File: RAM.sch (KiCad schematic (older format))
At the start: 2 parts, among them U1 STM32MP151AAB3, U2 MT41K64M16TW-107_AAT_J_TR

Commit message: Finish labelling RAM
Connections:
- net UDQS_N: now reaches U2.B7 (*UDQS)
- net UDQS: now reaches U2.C7 (UDQS)
- net UDM: now reaches U2.D3 (UDM)
- net LDM: now reaches U2.E7 (LDM)
- net LDQS_P: now reaches U2.F3 (LDQS)
- net LDQS_N: now reaches U2.G3 (*LDQS)
- net VREFDQ: now reaches U2.H1 (VREFDQ)
- net RAS_N: now reaches U2.J3 (*RAS)
- net CK_P: now reaches U2.J7 (CK)
- net ODT: now reaches U2.K1 (ODT)
- net ODT: now also U1.H19 (DDR_ODT)
- net CAS_N: now reaches U2.K3 (*CAS)
- net CK_N: now reaches U2.K7 (*CK)
- net CKE: now reaches U2.K9 (CKE)
- net CKE: now also U1.P19 (DDR_CKE)
- net CS_N: now reaches U2.L2 (*CS)
- net CS_N: now also U1.J18 (DDR_CSN)
- net WE_N: now reaches U2.L3 (*WE)
- net WE_N: now also U1.J17 (DDR_WEN)
- net ZQ: now reaches U2.L8 (ZQ)
- net ZQ: now also U1.F18 (DDR_ZQ)
- net VREFCA: now reaches U2.M8 (VREFCA)
- net RESET_N: now reaches U2.T2 (*RESET)
- net RESET_N: now also U1.G16 (DDR_RESETN)
- net VDD renamed VDDR
- no-connect marks 0 -> 1
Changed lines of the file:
@@
 U 1 1 60175F93
 P 1000 1400
-F 0 "U?" H 2600 1887 60  0000 C CNN
+F 0 "U2" H 2600 1887 60  0000 C CNN
 F 1 "MT41K64M16TW-107_AAT_J_TR" H 2600 1781 60  0000 C CNN
 F 2 "LinuxBoard:MT41K64M16TW-107_AAT_J_TR" H 2600 1740 60  0001 C CNN
@@
 AR Path="/601728E9/6049E2E1" Ref="U?"  Part="4"
 AR Path="/60172A77/6049E2E1" Ref="U1"  Part="4"
-F 0 "U?" H 9400 1787 60  0000 C CNN
+F 0 "U1" H 9400 1787 60  0000 C CNN
 F 1 "STM32MP151AAB3" H 9400 1681 60  0000 C CNN
 F 2 "LinuxBoard:STM32MP151AAB3" H 8550 1640 60  0001 C CNN
@@
 AR Path="/601728E9/6049E2E7" Ref="U?"  Part="3"
 AR Path="/60172A77/6049E2E7" Ref="U1"  Part="3"
-F 0 "U?" H 6150 1787 60  0000 C CNN
+F 0 "U1" H 6150 1787 60  0000 C CNN
 F 1 "STM32MP151AAB3" H 6150 1681 60  0000 C CNN
 F 2 "LinuxBoard:STM32MP151AAB3" H 5950 1640 60  0001 C CNN
@@
 	1350 7100 1350 7200
 $Comp
-L power:GND #PWR011
+L power:GND #PWR0101
 U 1 1 60844341
 P 1350 7200
-F 0 "#PWR?" H 1350 6950 50  0001 C CNN
+F 0 "#PWR0101" H 1350 6950 50  0001 C CNN
 F 1 "GND" H 1355 7027 50  0000 C CNN
 F 2 "" H 1350 7200 50  0001 C CNN
@@
 Text Label 1000 3200 2    50   ~ 0
 VDDQ
-Text Label 2100 7100 2    50   ~ 0
+Text Label 2200 7100 2    50   ~ 0
 VDD
 Text Label 1000 5400 2    50   ~ 0
@@
 	1000 7100 1000 7200
 $Comp
-L power:GND #PWR010
+L power:GND #PWR0102
 U 1 1 60E94F4D
 P 1000 7200
-F 0 "#PWR?" H 1000 6950 50  0001 C CNN
+F 0 "#PWR0102" H 1000 6950 50  0001 C CNN
 F 1 "GND" H 1005 7027 50  0000 C CNN
 F 2 "" H 1000 7200 50  0001 C CNN
@@
 	1    0    0    -1
 $EndComp
+Text Label 4200 5800 0    50   ~ 0
+CK_P
+Text Label 4200 5200 0    50   ~ 0
+CK_N
+Text Label 4200 5300 0    50   ~ 0
+CAS_N
+Text Label 4200 4700 0    50   ~ 0
+WE_N
+Text Label 4200 4800 0    50   ~ 0
+CS_N
+Text Label 1000 2400 2    50   ~ 0
+UDQS_N
+Text Label 1000 3500 2    50   ~ 0
+UDM
+Text Label 1000 3000 2    50   ~ 0
+UDQS
+Text Label 1000 4200 2    50   ~ 0
+LDM
+Text Label 1000 4700 2    50   ~ 0
+LDQS_P
+Text Label 1000 5300 2    50   ~ 0
+LDQS_N
+Text Label 4200 5900 0    50   ~ 0
+RAS_N
+Text Label 4200 5500 0    50   ~ 0
+ODT
+Text Label 4200 5000 0    50   ~ 0
+CKE
+Text HLabel 2400 7100 2    50   Input ~ 0
+VDDR
+Wire Wire Line
+	2400 7100 2200 7100
+Text Label 1000 5700 2    50   ~ 0
+VREFDQ
+NoConn ~ 1000 1400
+Text Label 4200 1800 0    50   ~ 0
+RESET_N
+Text Label 4200 3900 0    50   ~ 0
+VREFCA
+Text Label 4200 4500 0    50   ~ 0
+ZQ
+Text Label 8050 3500 2    50   ~ 0
+RESET_N
+Text Label 8050 1400 2    50   ~ 0
+ZQ
+Text Label 8050 1800 2    50   ~ 0
+CKE
+Text Label 8050 2400 2    50   ~ 0
+WE_N
+Text Label 8050 2200 2    50   ~ 0
+ODT
+Text Label 8050 2000 2    50   ~ 0
+CS_N
 $EndSCHEMATC

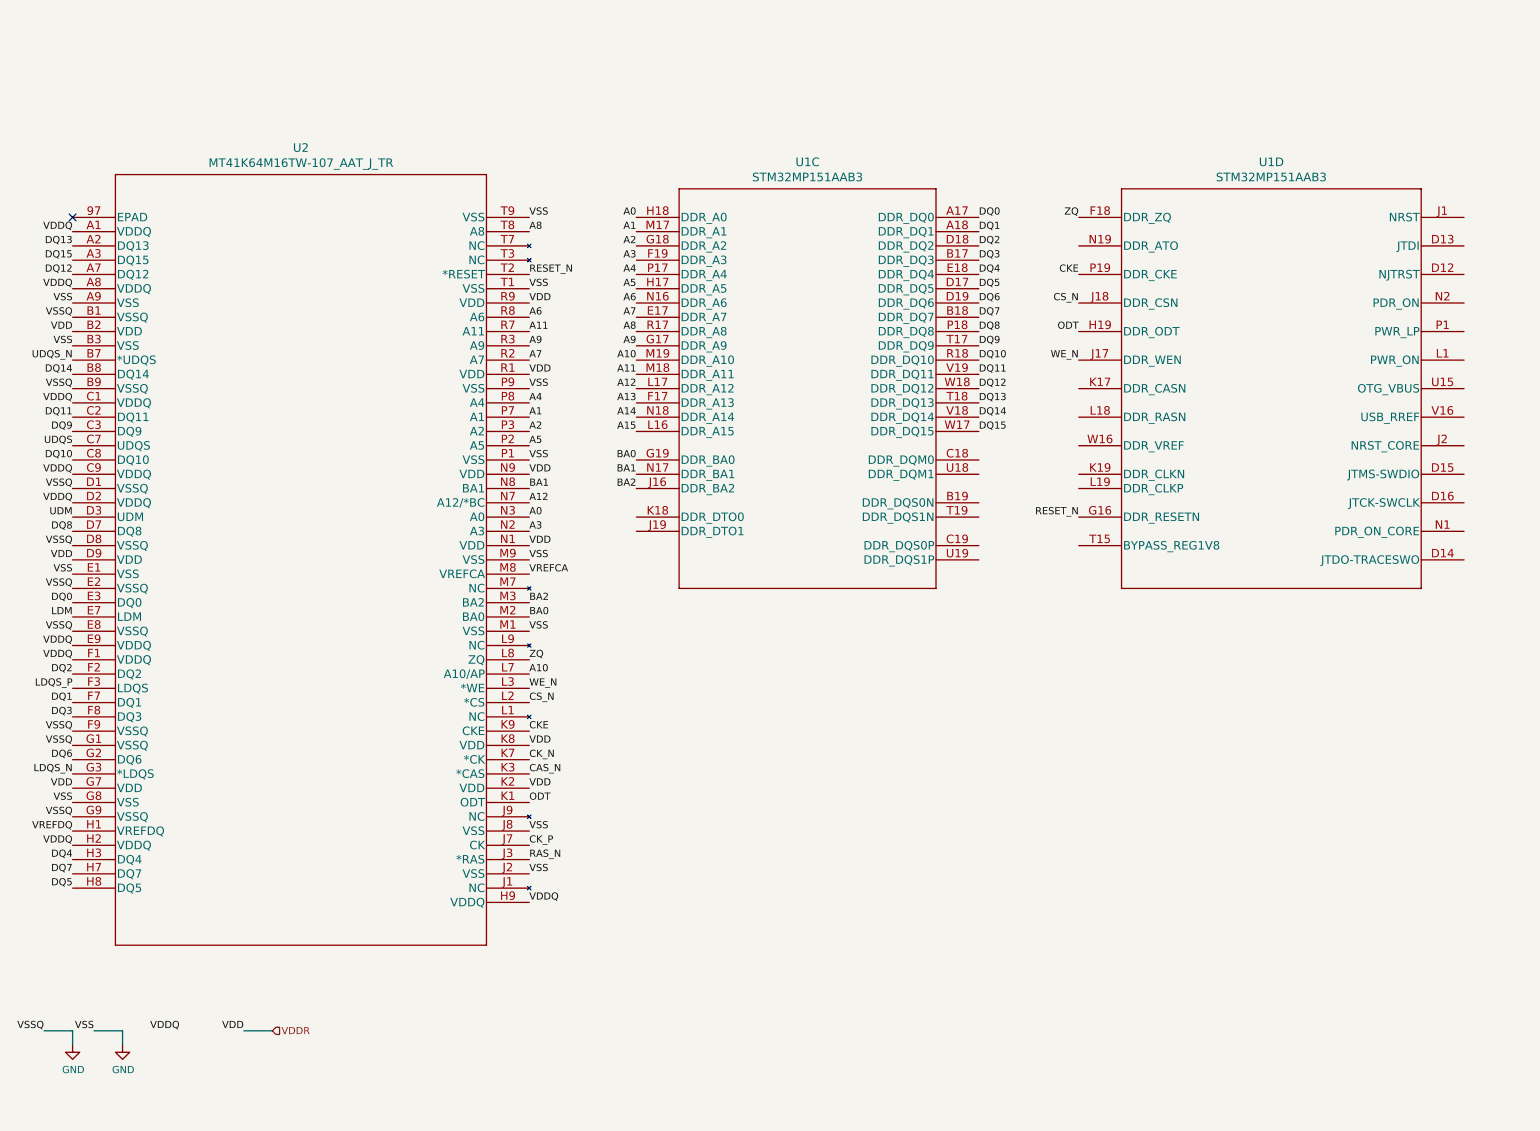
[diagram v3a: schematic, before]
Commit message: Finish DDR schematic
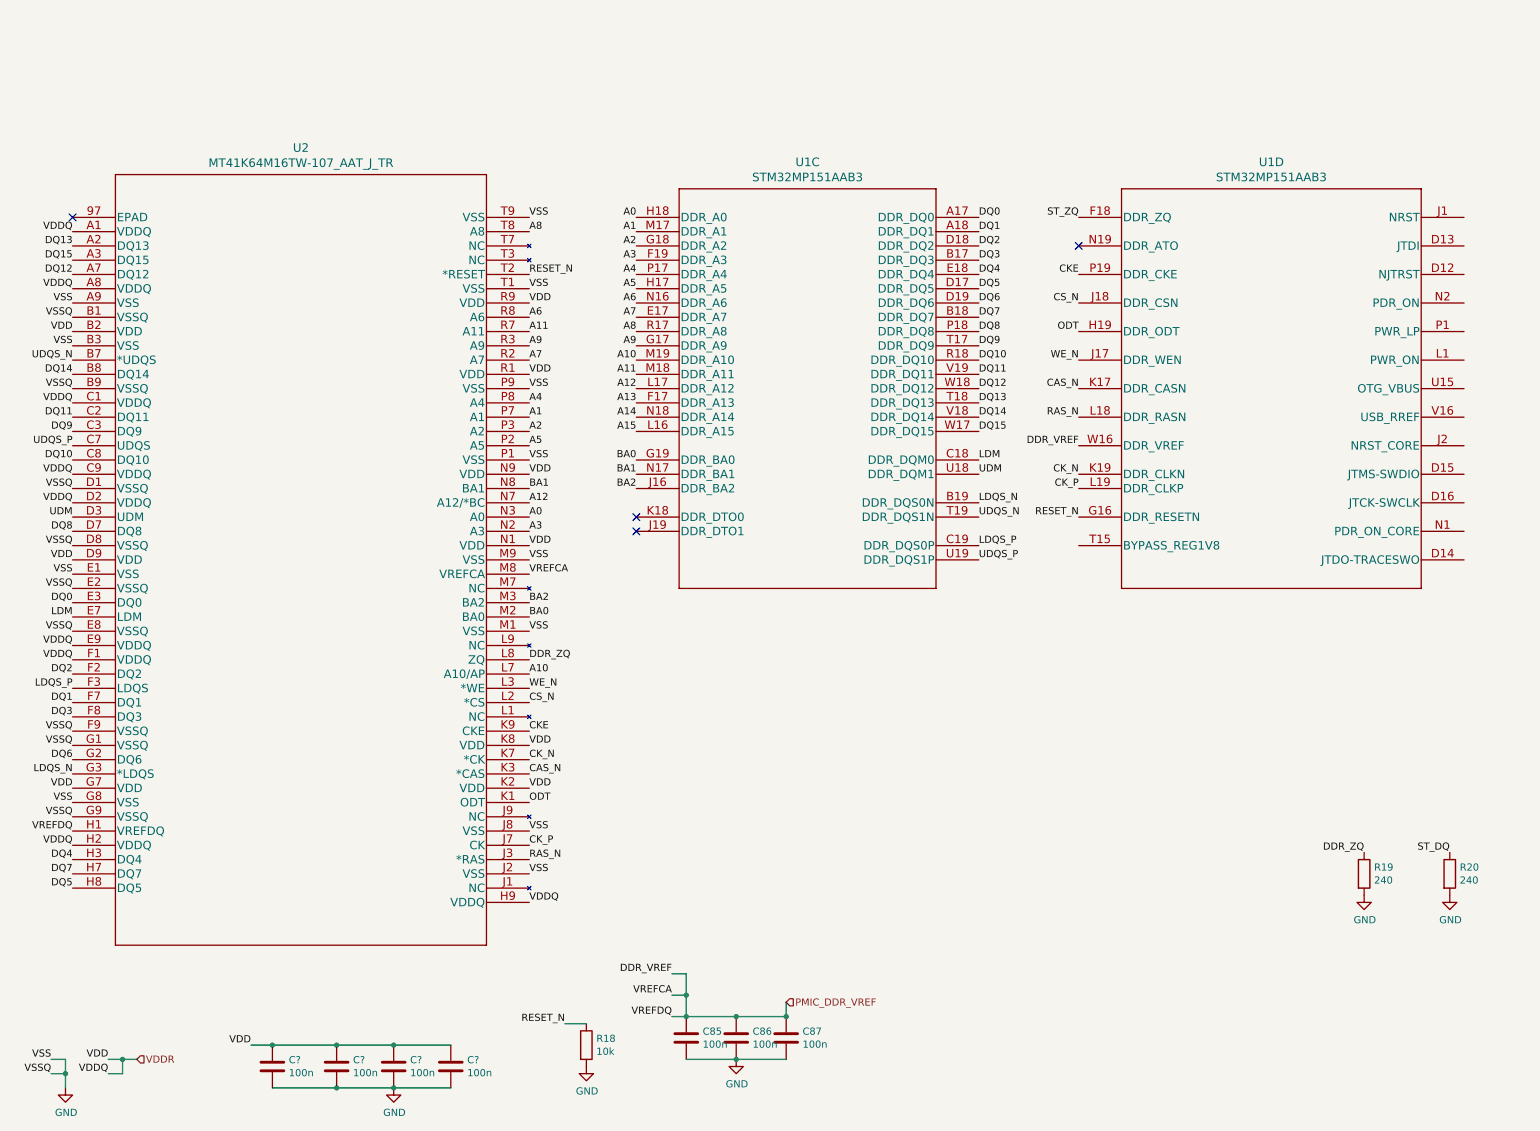
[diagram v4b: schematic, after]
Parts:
- added C85, C86, C87, C? (x4): 100n, symbol Device:C
- added R18: 10k, symbol Device:R
- added R19, R20: 240, symbol Device:R
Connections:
- net UDQS is gone; now on net UDQS_P: U2.C7 (UDQS)
- net VDDQ is gone; now on net VDDR: U2.A1 (VDDQ), U2.A8 (VDDQ), U2.C1 (VDDQ), U2.C9 (VDDQ), U2.D2 (VDDQ), U2.E9 (VDDQ), U2.F1 (VDDQ), U2.H2 (VDDQ), U2.H9 (VDDQ)
- net VREFCA is gone; now on net PMIC_DDR_VREF: U2.M8 (VREFCA)
- net VREFDQ is gone; now on net PMIC_DDR_VREF: U2.H1 (VREFDQ)
- net CAS_N: now also U1.K17 (DDR_CASN)
- net CK_N: now also U1.K19 (DDR_CLKN)
- net CK_P: now also U1.L19 (DDR_CLKP)
- net GND: now also C85.2, C86.2, C87.2, C?.2, C?.2, C?.2, C?.2, R18.2, R19.2, R20.2
- net LDM: now also U1.C18 (DDR_DQM0)
- net LDQS_N: now also U1.B19 (DDR_DQS0N)
- net LDQS_P: now also U1.C19 (DDR_DQS0P)
- net RAS_N: now also U1.L18 (DDR_RASN)
- net RESET_N: now also R18.1
- net UDM: now also U1.U18 (DDR_DQM1)
- net UDQS_N: now also U1.T19 (DDR_DQS1N)
- net VDDR: now also C?.1, C?.1, C?.1, C?.1
- net PMIC_DDR_VREF: now reaches U1.W16 (DDR_VREF)
- net PMIC_DDR_VREF: now also C85.1, C86.1, C87.1
- net UDQS_P: now reaches U1.U19 (DDR_DQS1P)
- net ZQ renamed DDR_ZQ
- net DDR_ZQ: now also R19.1; no longer U1.F18 (DDR_ZQ)
- new net ST_DQ: R20.1
- new net ST_ZQ: U1.F18 (DDR_ZQ)
- no-connect marks 1 -> 4

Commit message: Complete gpio selection, tidy sheets
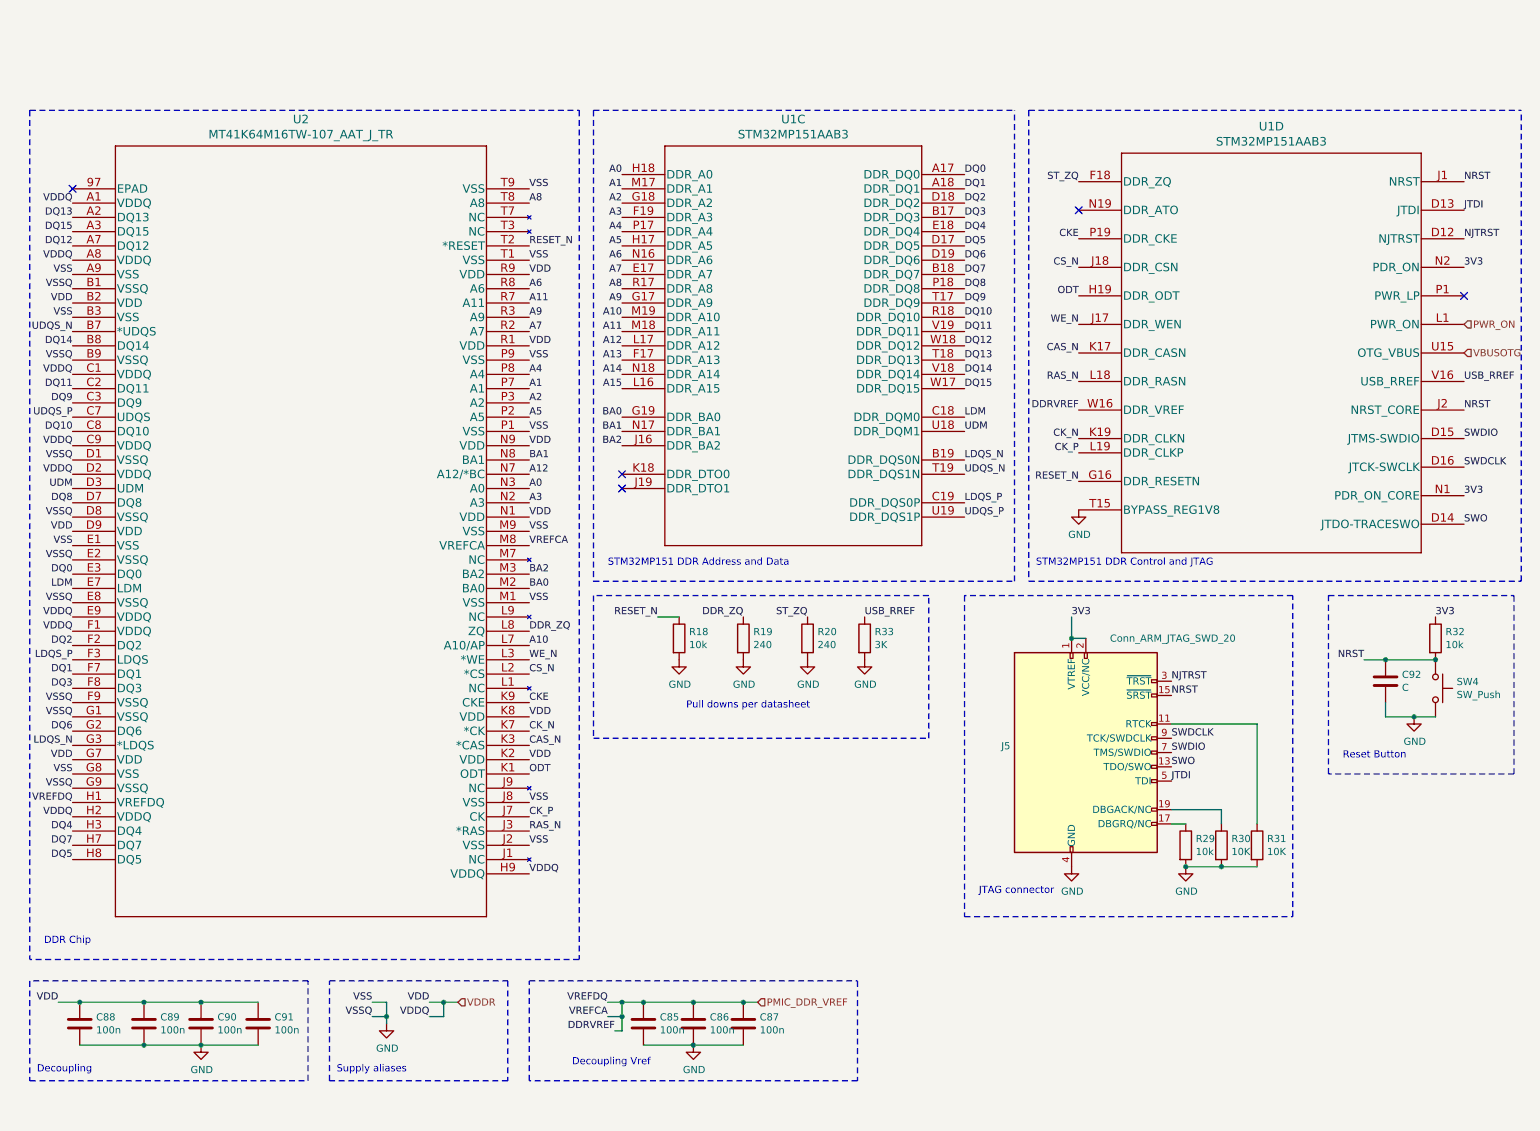
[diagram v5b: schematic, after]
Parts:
- added C92: C, symbol Device:C
- added J5: Conn_ARM_JTAG_SWD_20, symbol Connector:Conn_ARM_JTAG_SWD_20
- added R29, R32: 10k, symbol Device:R
- added R30, R31: 10K, symbol Device:R
- added R33: 3K, symbol Device:R
- added SW4: SW_Push, symbol Switch:SW_Push
- gave numbers to parts that had none: 4
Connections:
- net ST_DQ is gone; now on net ST_ZQ: R20.1
- net GND: now also U1.T15 (BYPASS_REG1V8), C92.2, J5.10 (GND), J5.12 (GND), J5.14 (GND), J5.16 (GND), J5.18 (GND), J5.20 (GND), J5.4 (GND), J5.6 (GND), J5.8 (GND), R29.2, R30.2, R31.2, R33.2, SW4.2
- net NJTRST: now reaches U1.D12 (NJTRST)
- net NJTRST: now also J5.3 (~TRST~)
- net JTDI: now reaches U1.D13 (JTDI)
- net JTDI: now also J5.5 (TDI)
- net SWO: now reaches U1.D14 (JTDO-TRACESWO)
- net SWO: now also J5.13 (TDO/SWO)
- net SWDIO: now reaches U1.D15 (JTMS-SWDIO)
- net SWDIO: now also J5.7 (TMS/SWDIO)
- net SWDCLK: now reaches U1.D16 (JTCK-SWCLK)
- net SWDCLK: now also J5.9 (TCK/SWDCLK)
- net NRST: now reaches U1.J1 (NRST)
- net NRST: now also U1.J2 (NRST_CORE), C92.1, J5.15 (~SRST~), R32.2, SW4.1
- net PWR_ON: now reaches U1.L1 (PWR_ON)
- net 3V3: now reaches U1.N1 (PDR_ON_CORE)
- net 3V3: now also U1.N2 (PDR_ON), J5.1 (VTREF), J5.2 (VCC/NC), R32.1
- net VBUSOTG: now reaches U1.U15 (OTG_VBUS)
- net USB_RREF: now reaches U1.V16 (USB_RREF)
- net USB_RREF: now also R33.1
- new net: J5.11 (RTCK), R31.1
- new net: J5.17 (DBGRQ/NC), R29.1
- new net: J5.19 (DBGACK/NC), R30.1
- no-connect marks 4 -> 5
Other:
- note added: "DDR Chip"
- note added: "Decoupling"
- note added: "Decoupling Vref"
- note added: "JTAG connector\n"
- note added: "Pull downs per datasheet"
- note added: "Reset Button\n"
- note added: "STM32MP151 DDR Address and Data"
- note added: "STM32MP151 DDR Control and JTAG"
- note added: "Supply aliases\n"
- moved on the sheet: C85, C86, C87, C88, C89, C90, C91, R18, R19, R20, U1C, U1D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

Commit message: Start crossing off ERC. Add generated BOM
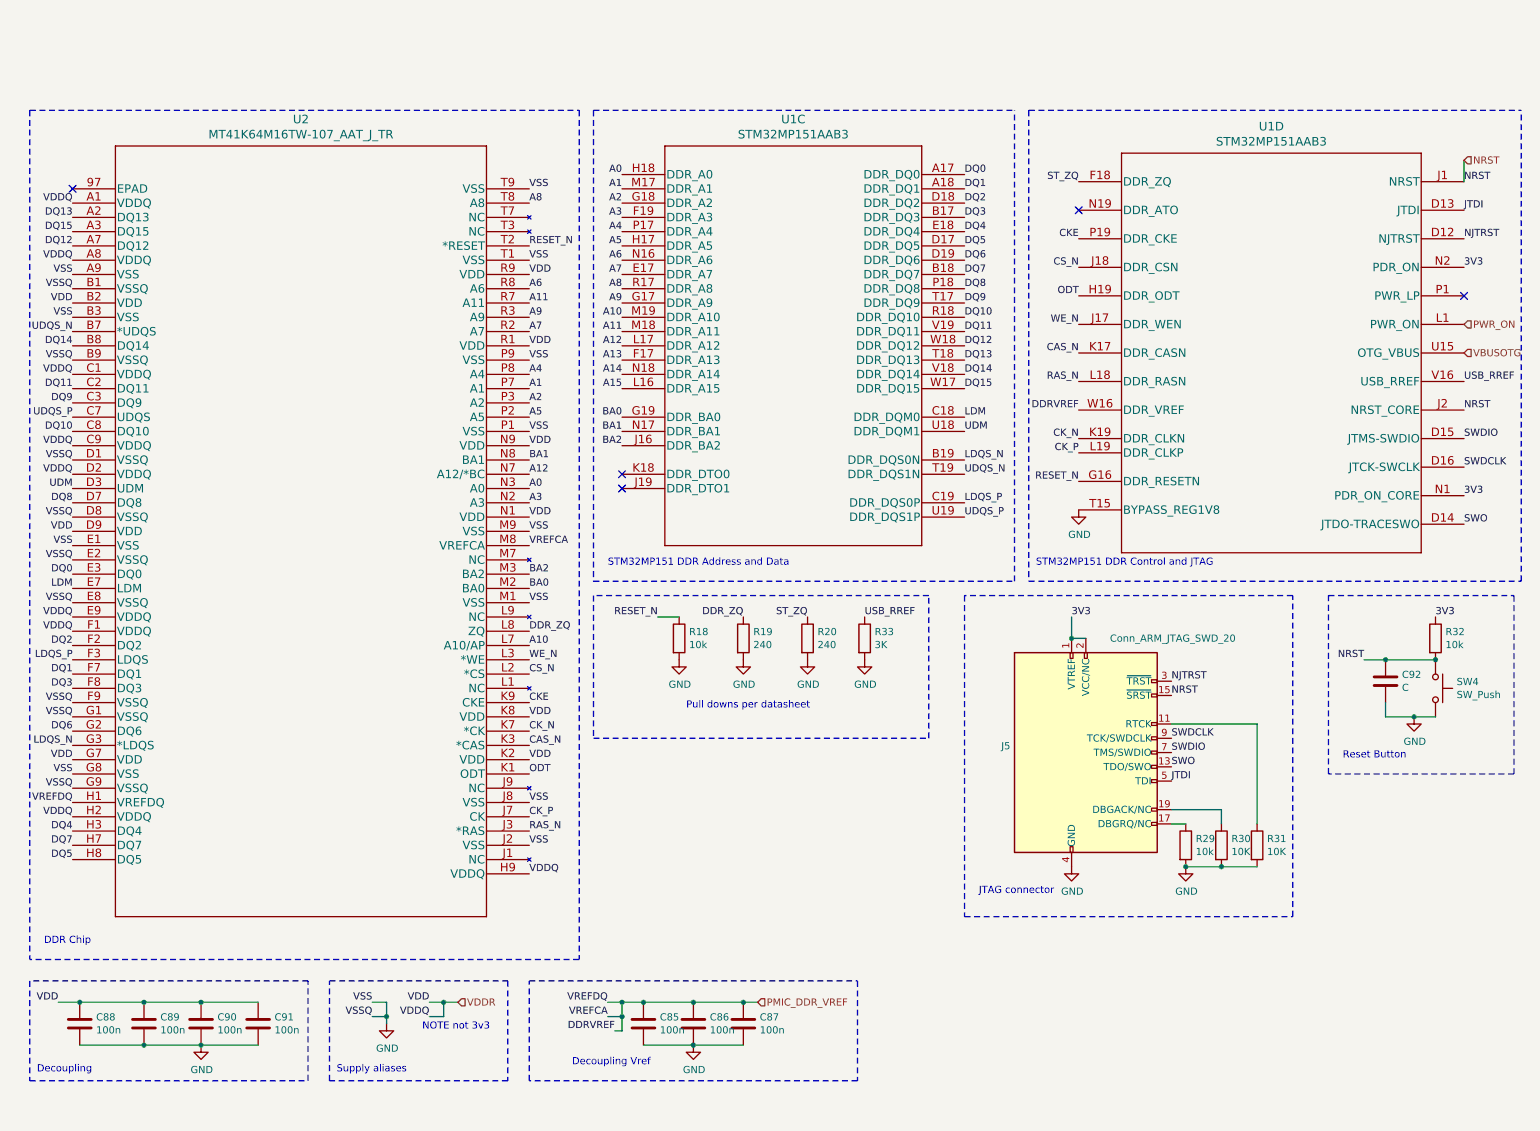
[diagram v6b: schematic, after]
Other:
- note added: "NOTE not 3v3\n"
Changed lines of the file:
@@
 Text HLabel 10750 2350 2    50   Input ~ 0
 VBUSOTG
+Text HLabel 10750 1000 2    50   Input ~ 0
+NRST
+Wire Wire Line
+	10750 1000 10750 1150
+Text Notes 3450 7100 0    50   ~ 0
+NOTE not 3v3\n
 $EndSCHEMATC
